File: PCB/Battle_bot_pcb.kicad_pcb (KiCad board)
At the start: 4 copper layers, 45.8 x 30.4 mm, 60 parts, among them J2 USB_C_Receptacle_USB2.0, J4 Conn_01x02, J5 Conn_01x02, J6 Conn_01x02, J7 Conn_01x02, J8 Conn_01x02, J9 Conn_01x04, SW1 Reset, SW2 Boot, U2 TPS62172DSG, U3 USBLC6-2P6, U5 LSM6DS3, U6 DRV8833RTY, U7 LM1117LD-3.3, U8 ESP32-S3, Y1 40MHz

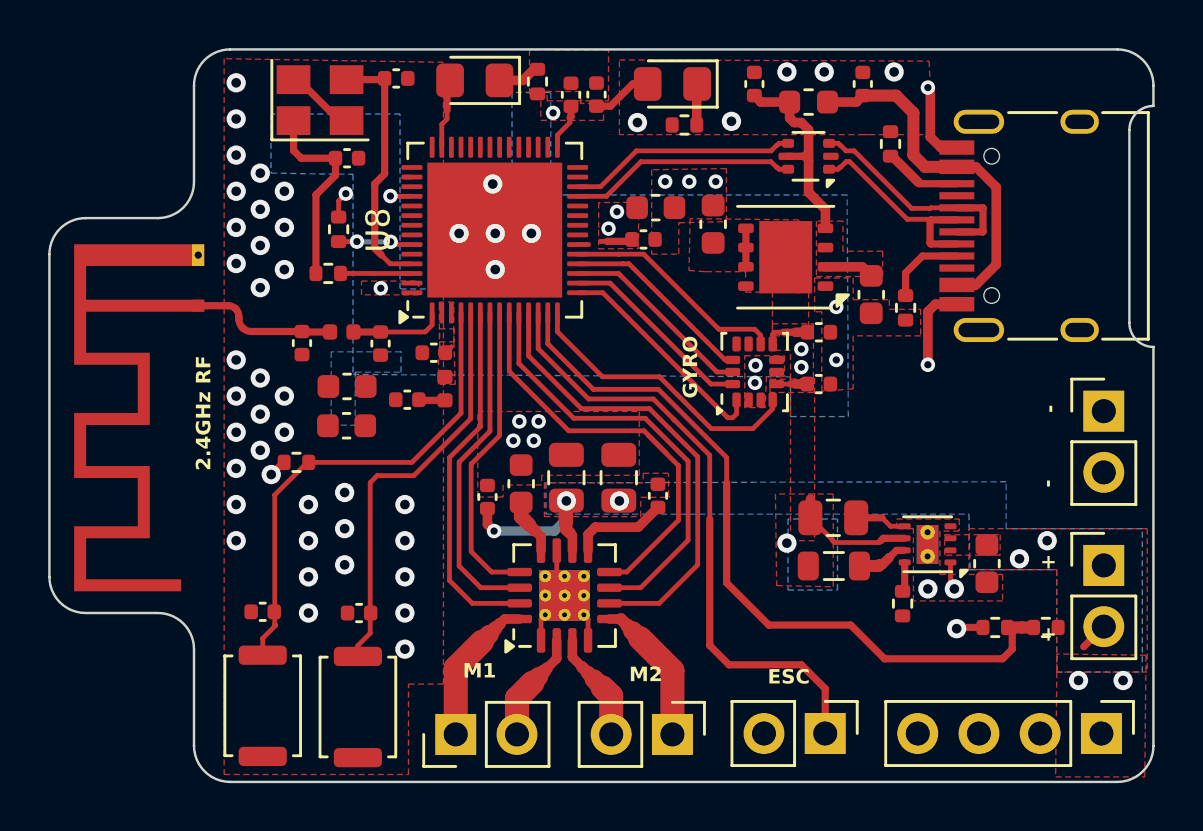
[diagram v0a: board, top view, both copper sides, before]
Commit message: Set up platfrom io for esp firmware development
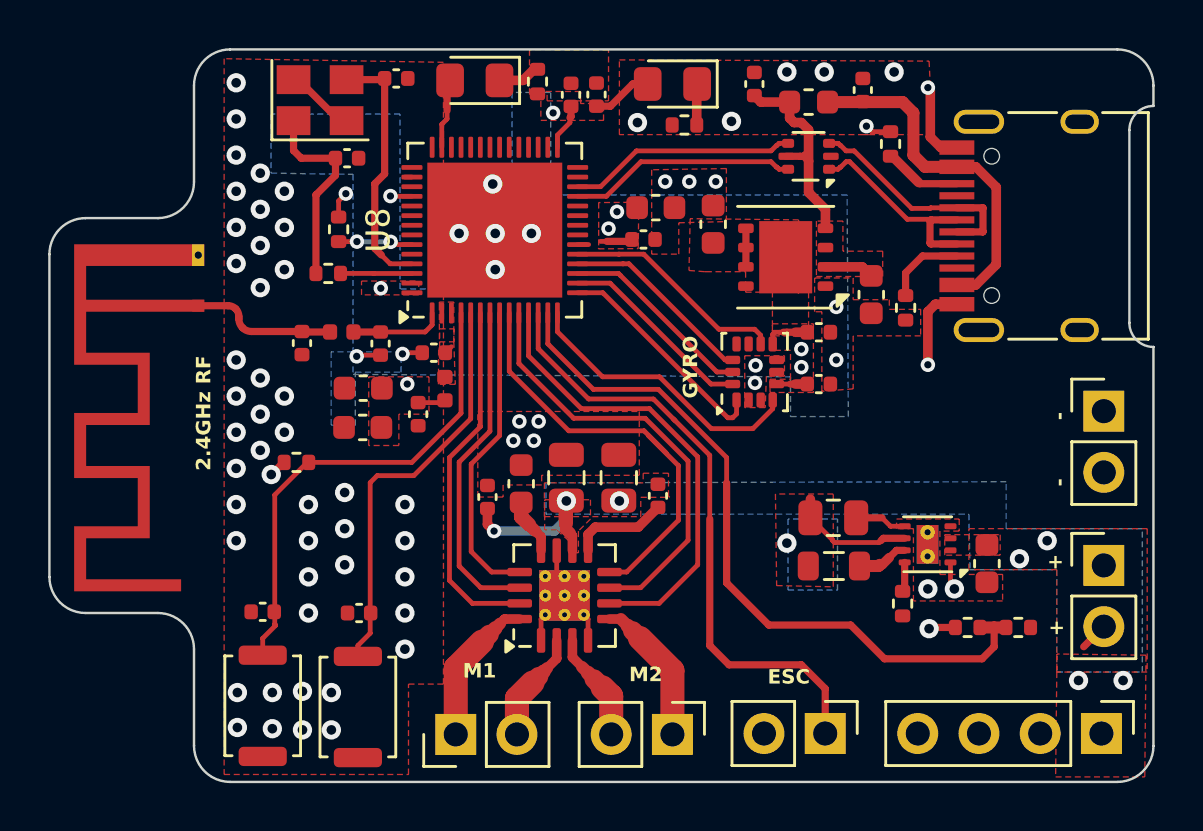
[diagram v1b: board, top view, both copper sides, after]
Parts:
- moved R5 1.15 mm to (160.4, 107.1)
- moved R8 1.15 mm to (158.4, 107.1)
- moved C8 0.75 mm to (135.6, 98.2), turned to -90 degrees
- moved C9 0.67 mm to (133.3, 97.2), turned to 180 degrees
- moved C26 0.67 mm to (133.2, 98.8), turned to 180 degrees
- moved C12 0.25 mm to (154.0, 84.8)
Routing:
- net GND: track 20.8 -> 23.7 mm, vias 62 -> 73
- net /Vsense: track 31.3 -> 30.3 mm
- net +3.3V: track 18.6 -> 18.7 mm, vias 9 -> 10

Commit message: Added Power multiplexer to schematic
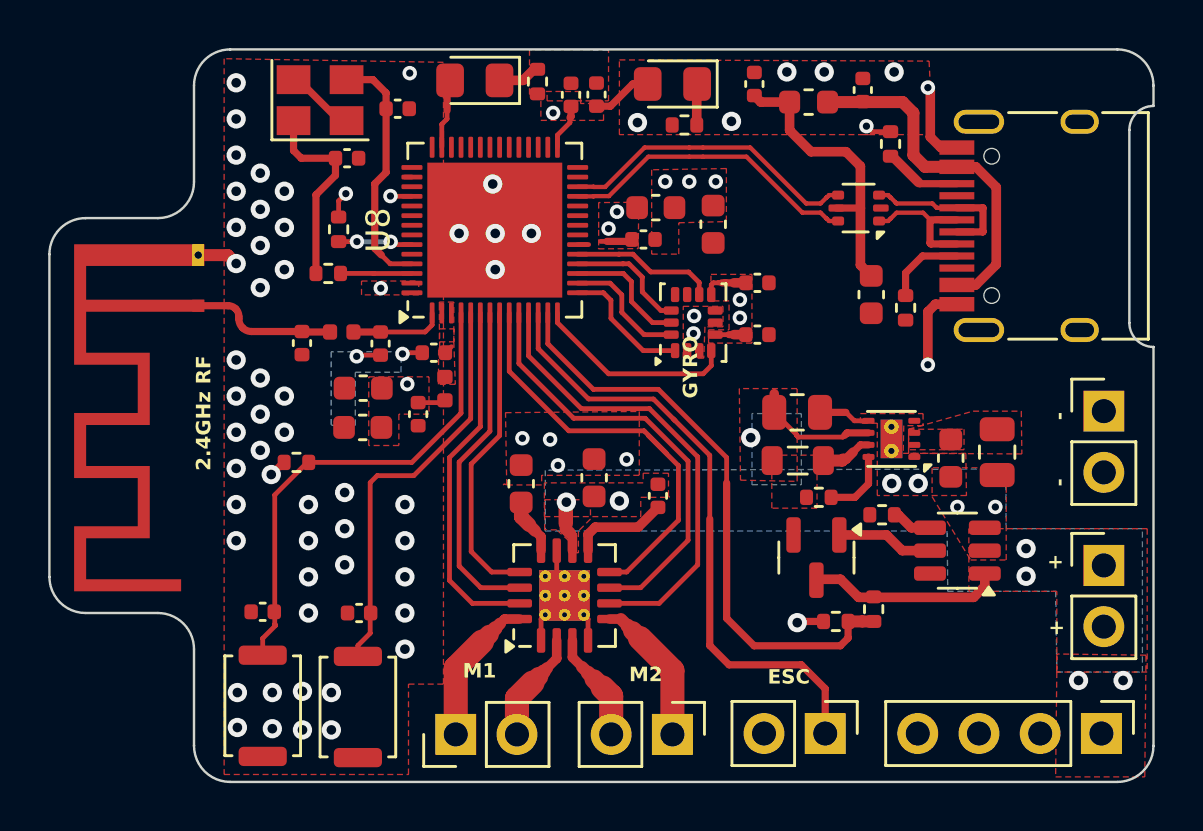
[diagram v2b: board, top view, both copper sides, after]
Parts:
- removed C16: 100n, Capacitor_SMD:C_0402_1005Metric
- removed U7: LM1117LD-3.3, Package_SON:WSON-8-1EP_4x4mm_P0.8mm_EP2.2x3mm
- added Q1: AO3401A, Package_TO_SOT_SMD:SOT-23, F.Cu at (152.1, 104.2)
- added R11: 470k, Resistor_SMD:R_0402_1005Metric, F.Cu at (154.8, 102.4)
- added U1: LTC4412xS6, Package_TO_SOT_SMD:TSOT-23-6, F.Cu at (157.9, 103.9)
- C22: value 22u -> 10u; footprint Capacitor_SMD:C_0805_2012Metric -> Capacitor_SMD:C_0603_1608Metric
- moved C11 17.9 mm to (159.6, 99.8), turned to -90 degrees
- moved R5 6.05 mm to (154.4, 106.3), turned to -90 degrees
- moved R4 5.61 mm to (152.2, 101.7), turned to 0 degrees
- moved R8 5.48 mm to (152.9, 106.8)
- moved C23 4.62 mm to (157.7, 100.1)
- moved C24 4.62 mm to (151.3, 98.2)
- moved L4 4.62 mm to (151.3, 100.2)
- moved U2 4.62 mm to (155.2, 99.3)
- moved C17 3.27 mm to (149.6, 92.8)
- moved C18 3.27 mm to (149.6, 95.0)
- moved U5 3.27 mm to (147.0, 94.5)
- moved U3 2.99 mm to (153.8, 89.7)
- moved C3 1.26 mm to (134.7, 85.6)
- moved C22 1.03 mm to (142.8, 100.9)
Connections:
- C11 pad 1: +BATT -> +5V
- C23 pad 1: +BATT -> +5V
- U2 pad 2: +BATT -> +5V
- U2 pad 3: +BATT -> +5V
- U6 pad 13: /IN2 -> unconnected-(U6-AIN2-Pad13)
- U6 pad 14: /IN1 -> unconnected-(U6-AIN1-Pad14)
- U6 pad 7: /IN3 -> unconnected-(U6-BIN1-Pad7)
- U6 pad 8: /IN4 -> unconnected-(U6-BIN2-Pad8)
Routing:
- net /Vsense: track 30.3 -> 24.7 mm
- net Net-(Q1-G): track 0.00 -> 4.03 mm
- net /SDO: track 9.39 -> 5.48 mm
- net /INT1: track 12.1 -> 8.43 mm
- net /INT2: track 9.35 -> 6.03 mm
- net /D+: track 9.78 -> 6.61 mm
- net /USB_D-: track 9.46 -> 12.6 mm
- net /USB_D+: track 9.48 -> 12.6 mm
- net /CS: track 8.09 -> 5.05 mm
- net /SDA: track 8.17 -> 5.19 mm
- net /SCL: track 8.13 -> 5.21 mm
- net /STAT: track 0.00 -> 1.70 mm
- net Net-(U2-PG): track 1.24 -> 2.90 mm
- net +BATT: track 8.56 -> 10.2 mm, vias 7 -> 6
- net +3.3V: track 18.7 -> 17.1 mm
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
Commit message: Added schottky diode to power multiplexer to protect USB hardware
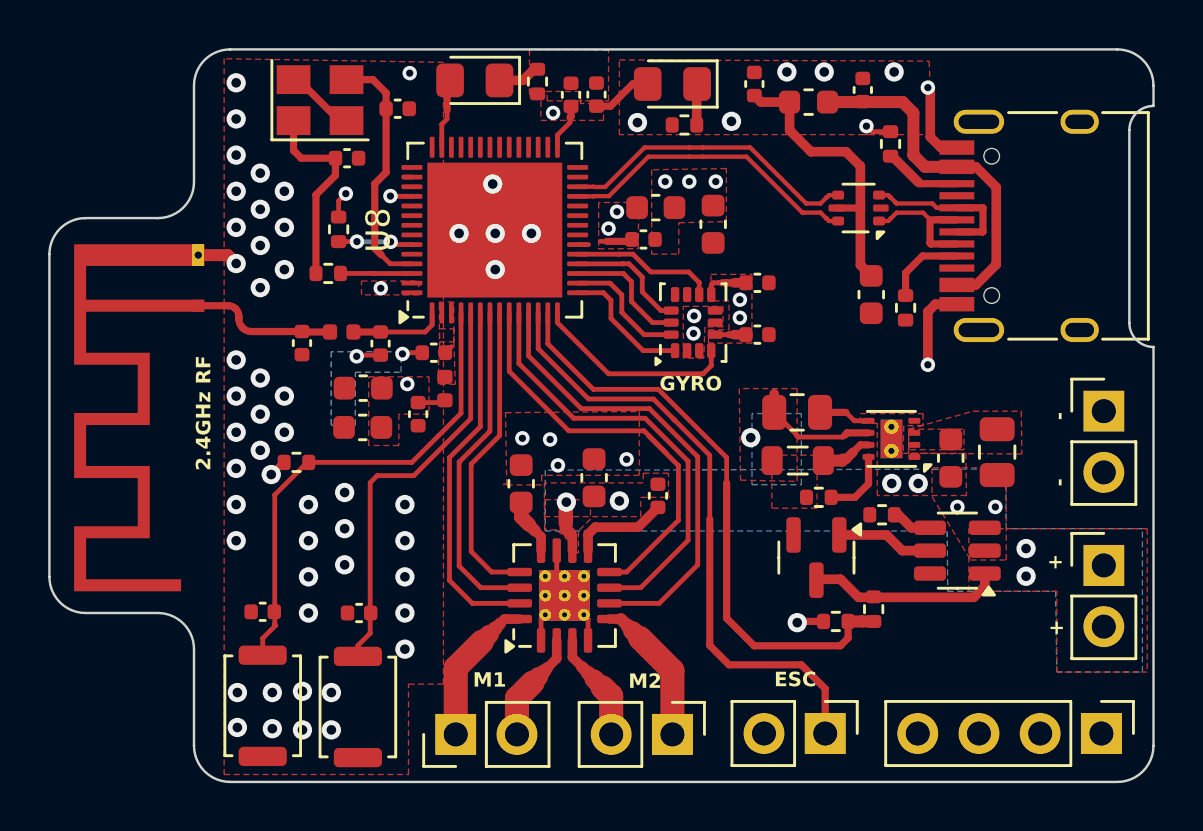
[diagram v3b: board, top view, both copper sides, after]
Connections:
- J9 pad 1: +BATT -> +3.3V
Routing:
- net +BATT: vias 6 -> 4
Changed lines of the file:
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@@
 		(tags "resistor")
 		(property "Reference" "R4"
-			(at 0 -1.17 360)
+			(at 0 -1.17 0)
 			(layer "F.SilkS")
 			(hide yes)
@@
 		)
 		(property "Value" "100k"
-			(at 0 1.17 360)
+			(at 0 1.17 0)
 			(layer "F.Fab")
 			(effects
@@
 		)
 		(fp_text user "${REFERENCE}"
-			(at 0 0 360)
+			(at 0 0 0)
 			(layer "F.Fab")
 			(effects
@@
 		(tags "TSOT TO_SOT_SMD")
 		(property "Reference" "U1"
-			(at 0 -2.4 360)
+			(at 0 -2.4 0)
 			(layer "F.SilkS")
 			(hide yes)
@@
 		)
 		(property "Value" "LTC4412xS6"
-			(at 0 2.4 360)
+			(at 0 2.4 0)
 			(layer "F.Fab")
 			(effects
@@
 		)
 		(property "Footprint" "Package_TO_SOT_SMD:TSOT-23-6"
-			(at 0 0 360)
+			(at 0 0 0)
 			(layer "F.Fab")
 			(hide yes)
@@
 		)
 		(property "Datasheet" "https://www.analog.com/media/en/technical-documentation/data-sheets/4412fb.pdf"
-			(at 0 0 360)
+			(at 0 0 0)
 			(layer "F.Fab")
 			(hide yes)
@@
 		)
 		(property "Description" "Low Loss PowerPath Controller, TSOT-23-6"
-			(at 0 0 360)
+			(at 0 0 0)
 			(layer "F.Fab")
 			(hide yes)
@@
 		)
 		(fp_text user "${REFERENCE}"
-			(at 0 0 360)
+			(at 0 0 0)
 			(layer "F.Fab")
 			(effects
@@
 		(tags "resistor")
 		(property "Reference" "R11"
-			(at 0 -1.17 360)
+			(at 0 -1.17 0)
 			(layer "F.SilkS")
 			(hide yes)
@@
 		)
 		(property "Value" "470k"
-			(at 0 1.17 360)
+			(at 0 1.17 0)
 			(layer "F.Fab")
 			(effects
@@
 		)
 		(fp_text user "${REFERENCE}"
-			(at 0 0 360)
+			(at 0 0 0)
 			(layer "F.Fab")
 			(effects
@@
 			(layers "*.Cu" "*.Mask")
 			(remove_unused_layers no)
-			(net 45 "+BATT")
+			(net 1 "+3.3V")
 			(pinfunction "Pin_1")
 			(pintype "passive")
@@
 	)
 	(gr_text "ESC"
-		(at 150.05 109.5 0)
+		(at 150.32 109.61 0)
 		(layer "F.SilkS" knockout)
 		(effects
@@
 	)
 	(gr_text "GYRO"
-		(at 147.2 97.6 90)
+		(at 145.56 97.34 0)
 		(layer "F.SilkS" knockout)
 		(effects
@@
 	)
 	(gr_text "M1"
-		(at 137.4 109.25 0)
+		(at 137.82 109.63 0)
 		(layer "F.SilkS" knockout)
 		(effects
@@
 	)
 	(gr_text "M2"
-		(at 144.3 109.4 0)
+		(at 144.27 109.68 0)
 		(layer "F.SilkS" knockout)
 		(effects
@@
 	)
 	(via
-		(at 164.8 109.3)
-		(size 0.8)
-		(drill 0.4)
-		(layers "F.Cu" "B.Cu")
-		(free yes)
-		(net 45)
-	)
-	(via
 		(at 143.9 101.85)
 		(size 0.8)
@@
 		(net 45)
 	)
-	(via
-		(at 162.95 109.3)
-		(size 0.8)
-		(drill 0.4)
-		(layers "F.Cu" "B.Cu")
-		(free yes)
-		(net 45)
-	)
 	(segment
 		(start 136.85 105.15)
@@
 			)
 		)
-	)
-	(zone
-		(net 45)
-		(net_name "+BATT")
-		(layer "F.Cu")
-		(hatch edge 0.5)
-		(priority 13)
-		(connect_pads yes
-			(clearance 0.2)
-		)
-		(min_thickness 0.25)
-		(filled_areas_thickness no)
-		(fill yes
-			(thermal_gap 0.5)
-			(thermal_bridge_width 0.5)
-		)
-		(polygon
-			(pts
-				(xy 162.05 108.95) (xy 162 113.3) (xy 165.7 113.3) (xy 165.75 108.25) (xy 162.05 108.2)
-			)
-		)

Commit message: added ESD Protection Diode near MCU
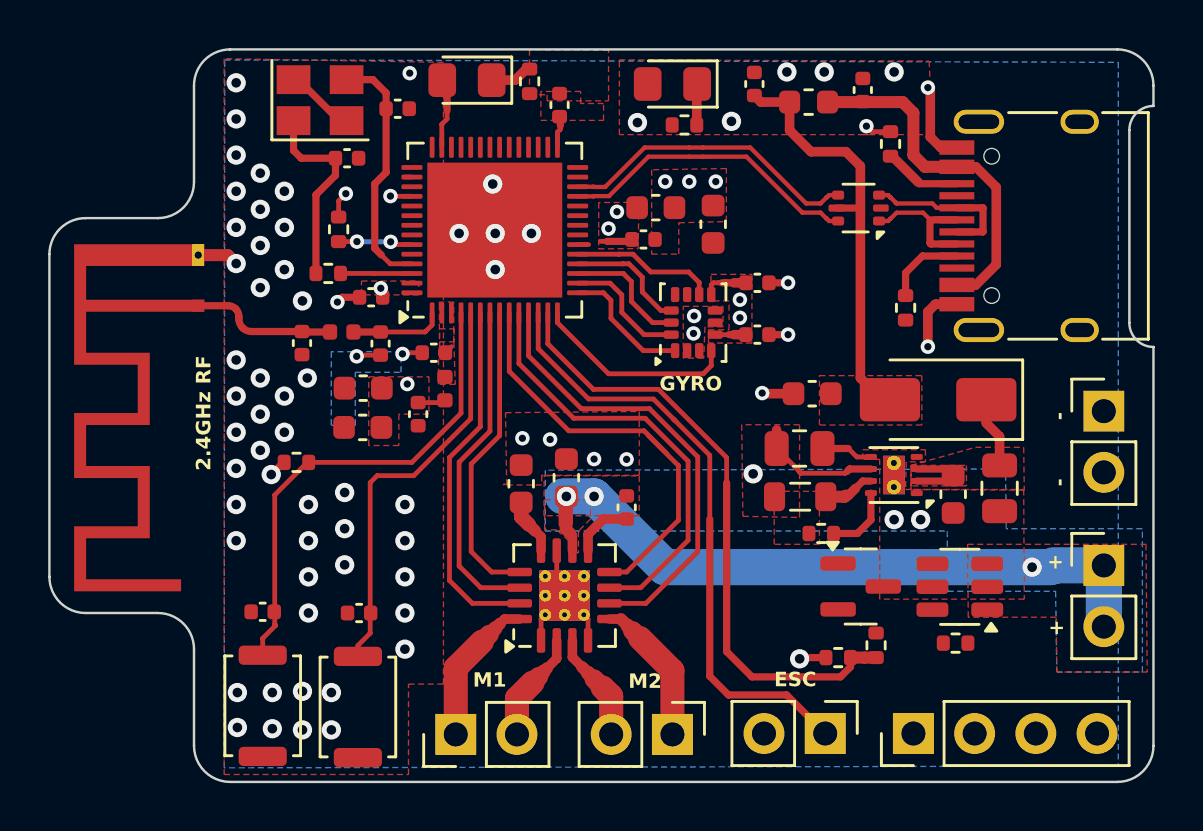
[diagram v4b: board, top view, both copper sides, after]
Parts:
- added D3: SS14, Diode_SMD:D_SMA, F.Cu at (157.1, 97.7)
- moved C21 12.6 mm to (133.6, 93.4), turned to 180 degrees
- moved J9 7.80 mm to (156.1, 111.5), turned to 90 degrees
- moved R11 6.14 mm to (157.8, 107.8)
- moved C14 4.79 mm to (151.9, 97.4), turned to 180 degrees
- moved Q1 2.19 mm to (153.9, 105.4), turned to 0 degrees
- moved C11 1.50 mm to (159.7, 101.3)
- moved R5 1.50 mm to (154.6, 107.8)
- moved C23 1.50 mm to (157.8, 101.6)
- moved C24 1.50 mm to (151.4, 99.7)
- moved L4 1.50 mm to (151.4, 101.7)
- moved R4 1.50 mm to (152.3, 103.2)
- moved R8 1.50 mm to (153.0, 108.3)
- moved U1 1.50 mm to (158.0, 105.4)
- moved U2 1.50 mm to (155.3, 100.8)
- moved C19 1.39 mm to (144.2, 102.1)
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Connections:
- C11 pad 1: +5V -> /LOAD
- C23 pad 1: +5V -> /LOAD
- Q1 pad 2: +5V -> /LOAD
- U1 pad 6: +5V -> /LOAD
- U2 pad 2: +5V -> /LOAD
- U2 pad 3: +5V -> /LOAD
- U8 pad 23: unconnected-(U8-GPIO17/ADC2_CH6-Pad23) -> /STAT
- U8 pad 49: unconnected-(U8-U0TXD/PROG/GPIO43-Pad49) -> /TX
- U8 pad 50: /TX -> /RX
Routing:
- net +BATT: track 10.2 -> 28.7 mm, vias 4 -> 3
- net /LOAD: track 0.00 -> 6.18 mm
- net +5V: track 12.0 -> 17.7 mm
- net Net-(Q1-G): track 4.03 -> 0.00 mm
- net GND: track 24.5 -> 27.7 mm, vias 74 -> 78
- net +3.3V: track 17.1 -> 15.0 mm, vias 10 -> 9
- net /STAT: track 1.70 -> 0.00 mm
- net Net-(U6-VCP): track 4.04 -> 2.54 mm
- net /Vsense: track 24.7 -> 25.9 mm
- added copper zone on F.Cu, net /LOAD
- added copper zone on In2.Cu, net GND
- removed copper zone on In2.Cu, net +3.3V
